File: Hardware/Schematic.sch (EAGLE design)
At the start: 48 parts, among them IC1 XC6220A331MR-G, J1 SAMACSYS_PARTS_USB4110-GF-A, J2 FH34SRJ-24S-0.5SH_99_, J4 112A-TAAR-R03_ATTEND, Q1 20V/4.2A/52mΩ/1.4W, Q2 SI1308EDL-T1-GE3, Q3 20V/4.2A/52mΩ/1.4W, U1 ESP32_WROVER_SPARKFUN-IC-POWE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, U2 ESP32-C6-WROOM-1-N8

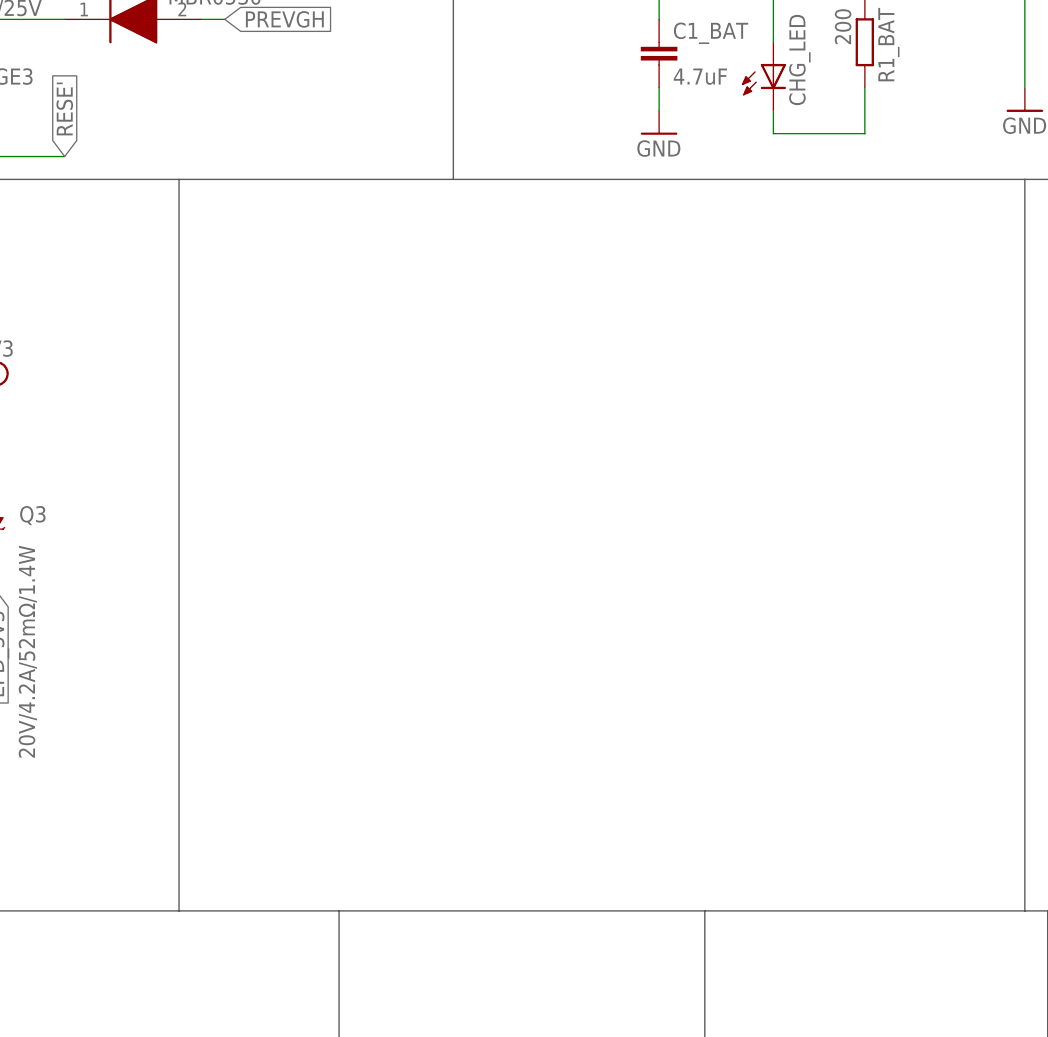
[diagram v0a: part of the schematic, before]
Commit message: add Environmental Sensor BME688
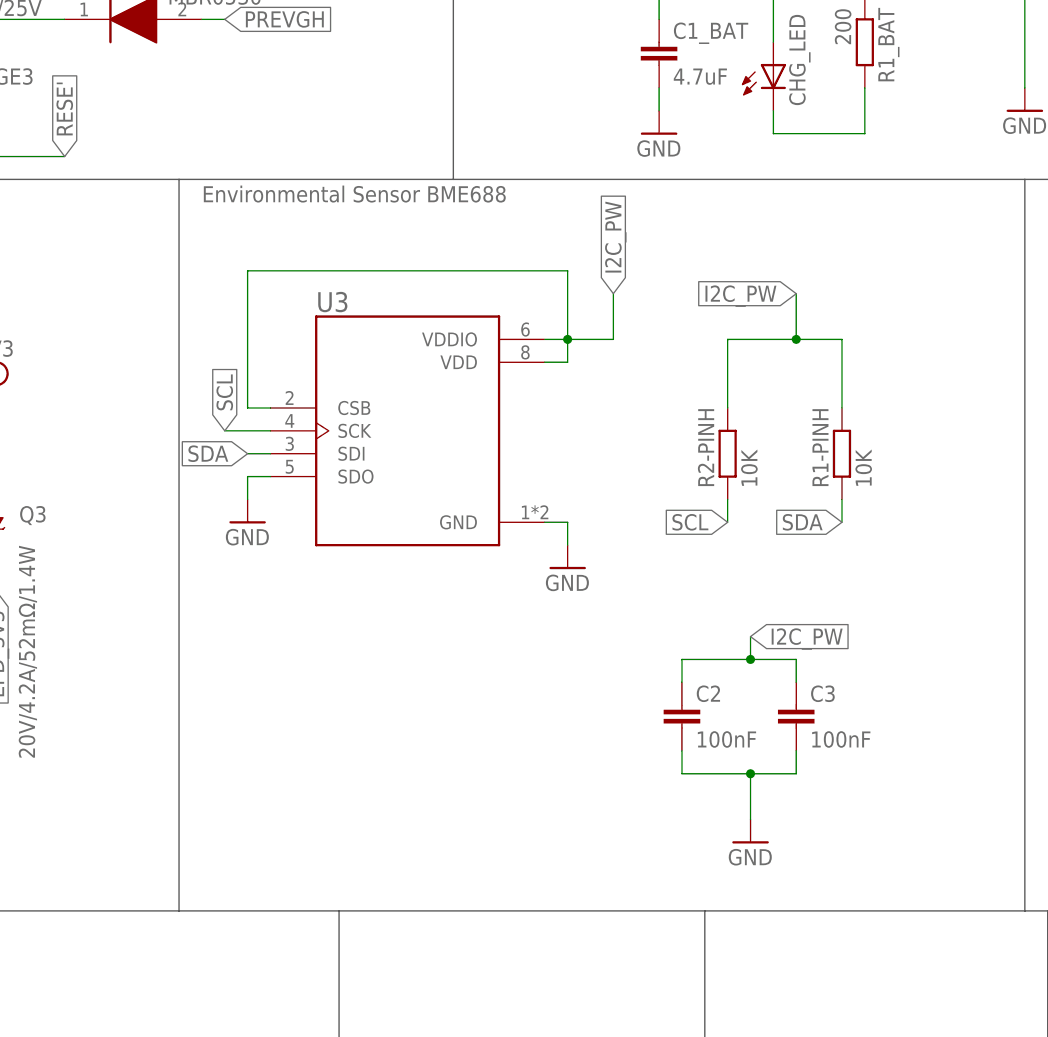
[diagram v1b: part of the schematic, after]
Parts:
- added C2, C3: 100nF, DeskAssistant v19 v1.flbr:ESP32_WROVER_EAGLE-LTSPICE_CC0402
- added R1-PINH, R2-PINH: 10K, DeskAssistant v19 v1.flbr:ESP32_WROVER_EAGLE-LTSPICE_RR0402
- added U3: ESP32_WROVER_BME680_BME680, DeskAssistant v19 v1.flbr:ESP32_WROVER_BME680_BME680
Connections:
- net GND: now also C2.2, C3.2, U3.GND, U3.SDO
- net I2C_PW: now also C2.1, C3.1, R1-PINH.2, R2-PINH.2, U3.CSB, U3.VDD, U3.VDDIO
- net SCL: now also R2-PINH.1, U3.SCK
- net SDA: now also R1-PINH.1, U3.SDI
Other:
- note added: "Environmental Sensor BME688"
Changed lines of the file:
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@@
 <part name="SUPPLY6" library="DeskAssistant v19 v1.flbr" library_urn="urn:adsk.wipprod:fs.file:vf.vVvdDOfaSfavM5thX5SjWw" deviceset="3V3-CIRCLE" device="" value="3V3"/>
 <part name="R_CL1" library="DeskAssistant v19 v1.flbr" library_urn="urn:adsk.wipprod:fs.file:vf.vVvdDOfaSfavM5thX5SjWw" deviceset="ESP32_WROVER_EAGLE-LTSPICE_R" device="R0402" value="10K"/>
+<part name="U3" library="DeskAssistant v19 v1.flbr" library_urn="urn:adsk.wipprod:fs.file:vf.vVvdDOfaSfavM5thX5SjWw" deviceset="ESP32_WROVER_BME680_BME680" device=""/>
+<part name="GND27" library="DeskAssistant v19 v1.flbr" library_urn="urn:adsk.wipprod:fs.file:vf.vVvdDOfaSfavM5thX5SjWw" deviceset="GND" device=""/>
+<part name="GND28" library="DeskAssistant v19 v1.flbr" library_urn="urn:adsk.wipprod:fs.file:vf.vVvdDOfaSfavM5thX5SjWw" deviceset="GND" device=""/>
+<part name="R2-PINH" library="DeskAssistant v19 v1.flbr" library_urn="urn:adsk.wipprod:fs.file:vf.vVvdDOfaSfavM5thX5SjWw" deviceset="ESP32_WROVER_EAGLE-LTSPICE_R" device="R0402" value="10K"/>
+<part name="R1-PINH" library="DeskAssistant v19 v1.flbr" library_urn="urn:adsk.wipprod:fs.file:vf.vVvdDOfaSfavM5thX5SjWw" deviceset="ESP32_WROVER_EAGLE-LTSPICE_R" device="R0402" value="10K"/>
+<part name="C2" library="DeskAssistant v19 v1.flbr" library_urn="urn:adsk.wipprod:fs.file:vf.vVvdDOfaSfavM5thX5SjWw" deviceset="ESP32_WROVER_EAGLE-LTSPICE_C" device="C0402" value="100nF"/>
+<part name="C3" library="DeskAssistant v19 v1.flbr" library_urn="urn:adsk.wipprod:fs.file:vf.vVvdDOfaSfavM5thX5SjWw" deviceset="ESP32_WROVER_EAGLE-LTSPICE_C" device="C0402" value="100nF"/>
+<part name="GND29" library="DeskAssistant v19 v1.flbr" library_urn="urn:adsk.wipprod:fs.file:vf.vVvdDOfaSfavM5thX5SjWw" deviceset="GND" device=""/>
 </parts>
 <sheets>
@@
 <text x="-160.02" y="165.1" size="1.778" layer="95">E-Paper Display Header</text>
 <text x="-73.66" y="162.56" size="1.778" layer="95">EPD Power</text>
+<text x="-27.94" y="165.1" size="1.778" layer="95">Environmental Sensor BME688</text>
 </plain>
 <instances>
@@
 <attribute name="NAME" x="-59.4614" y="146.05" size="1.778" layer="95" rot="R270"/>
 <attribute name="VALUE" x="-64.262" y="146.05" size="1.778" layer="96" rot="R270"/>
+</instance>
+<instance part="U3" gate="G$1" x="-5.08" y="139.7" smashed="yes">
+<attribute name="NAME" x="-15.2493" y="152.92" size="2.186390625" layer="95"/>
+</instance>
+<instance part="GND27" gate="1" x="12.7" y="124.46" smashed="yes">
+<attribute name="VALUE" x="10.16" y="121.92" size="1.778" layer="96"/>
+</instance>
+<instance part="GND28" gate="1" x="-22.86" y="129.54" smashed="yes">
+<attribute name="VALUE" x="-25.4" y="127" size="1.778" layer="96"/>
+</instance>
+<instance part="R2-PINH" gate="G$1" x="30.48" y="137.16" smashed="yes" rot="R90">
+<attribute name="NAME" x="28.9814" y="133.35" size="1.778" layer="95" rot="R90"/>
+<attribute name="VALUE" x="33.782" y="133.35" size="1.778" layer="96" rot="R90"/>
+<attribute name="NAME" x="28.9814" y="133.35" size="1.778" layer="95" rot="R90"/>
+<attribute name="VALUE" x="33.782" y="133.35" size="1.778" layer="96" rot="R90"/>
+</instance>
+<instance part="R1-PINH" gate="G$1" x="43.18" y="137.16" smashed="yes" rot="R90">
+<attribute name="NAME" x="41.6814" y="133.35" size="1.778" layer="95" rot="R90"/>
+<attribute name="VALUE" x="46.482" y="133.35" size="1.778" layer="96" rot="R90"/>
+<attribute name="NAME" x="41.6814" y="133.35" size="1.778" layer="95" rot="R90"/>
+<attribute name="VALUE" x="46.482" y="133.35" size="1.778" layer="96" rot="R90"/>
+</instance>
+<instance part="C2" gate="G$1" x="25.4" y="109.22" smashed="yes">
+<attribute name="NAME" x="26.924" y="109.601" size="1.778" layer="95"/>
+<attribute name="VALUE" x="26.924" y="104.521" size="1.778" layer="96"/>
+</instance>
+<instance part="C3" gate="G$1" x="38.1" y="109.22" smashed="yes">
+<attribute name="NAME" x="39.624" y="109.601" size="1.778" layer="95"/>
+<attribute name="VALUE" x="39.624" y="104.521" size="1.778" layer="96"/>
+</instance>
+<instance part="GND29" gate="1" x="33.02" y="93.98" smashed="yes">
+<attribute name="VALUE" x="30.48" y="91.44" size="1.778" layer="96"/>
 </instance>
 </instances>
@@
 <wire x1="-147.32" y1="144.78" x2="-149.86" y2="144.78" width="0.1524" layer="91"/>
 <pinref part="GND24" gate="1" pin="GND"/>
+</segment>
+<segment>
+<pinref part="U3" gate="G$1" pin="GND"/>
+<wire x1="10.16" y1="129.54" x2="12.7" y2="129.54" width="0.1524" layer="91"/>
+<wire x1="12.7" y1="129.54" x2="12.7" y2="127" width="0.1524" layer="91"/>
+<pinref part="GND27" gate="1" pin="GND"/>
+</segment>
+<segment>
+<pinref part="U3" gate="G$1" pin="SDO"/>
+<wire x1="-20.32" y1="134.62" x2="-22.86" y2="134.62" width="0.1524" layer="91"/>
+<wire x1="-22.86" y1="134.62" x2="-22.86" y2="132.08" width="0.1524" layer="91"/>
+<pinref part="GND28" gate="1" pin="GND"/>
+</segment>
+<segment>
+<pinref part="C2" gate="G$1" pin="2"/>
+<wire x1="25.4" y1="104.14" x2="25.4" y2="101.6" width="0.1524" layer="91"/>
+<wire x1="25.4" y1="101.6" x2="33.02" y2="101.6" width="0.1524" layer="91"/>
+<wire x1="33.02" y1="101.6" x2="38.1" y2="101.6" width="0.1524" layer="91"/>
+<wire x1="38.1" y1="101.6" x2="38.1" y2="104.14" width="0.1524" layer="91"/>
+<pinref part="C3" gate="G$1" pin="2"/>
+<junction x="33.02" y="101.6"/>
+<wire x1="33.02" y1="101.6" x2="33.02" y2="96.52" width="0.1524" layer="91"/>
+<pinref part="GND29" gate="1" pin="GND"/>
 </segment>
 </net>
@@
 <label x="190.5" y="195.58" size="1.778" layer="95" xref="yes"/>
 </segment>
+<segment>
+<pinref part="U3" gate="G$1" pin="VDDIO"/>
+<wire x1="10.16" y1="149.86" x2="12.7" y2="149.86" width="0.1524" layer="91"/>
+<wire x1="12.7" y1="149.86" x2="17.78" y2="149.86" width="0.1524" layer="91"/>
+<wire x1="17.78" y1="149.86" x2="17.78" y2="154.94" width="0.1524" layer="91"/>
+<pinref part="U3" gate="G$1" pin="VDD"/>
+<wire x1="10.16" y1="147.32" x2="12.7" y2="147.32" width="0.1524" layer="91"/>
+<wire x1="12.7" y1="147.32" x2="12.7" y2="149.86" width="0.1524" layer="91"/>
+<junction x="12.7" y="149.86"/>
+<wire x1="12.7" y1="149.86" x2="12.7" y2="157.48" width="0.1524" layer="91"/>
+<wire x1="12.7" y1="157.48" x2="-22.86" y2="157.48" width="0.1524" layer="91"/>
+<wire x1="-22.86" y1="157.48" x2="-22.86" y2="142.24" width="0.1524" layer="91"/>
+<wire x1="-22.86" y1="142.24" x2="-20.32" y2="142.24" width="0.1524" layer="91"/>
+<pinref part="U3" gate="G$1" pin="CSB"/>
+<label x="17.78" y="154.94" size="1.778" layer="95" rot="R90" xref="yes"/>
+</segment>
+<segment>
+<pinref part="R2-PINH" gate="G$1" pin="2"/>
+<wire x1="30.48" y1="142.24" x2="30.48" y2="149.86" width="0.1524" layer="91"/>
+<wire x1="30.48" y1="149.86" x2="38.1" y2="149.86" width="0.1524" layer="91"/>
+<wire x1="38.1" y1="149.86" x2="43.18" y2="149.86" width="0.1524" layer="91"/>
+<wire x1="43.18" y1="149.86" x2="43.18" y2="142.24" width="0.1524" layer="91"/>
+<pinref part="R1-PINH" gate="G$1" pin="2"/>
+<junction x="38.1" y="149.86"/>
+<wire x1="38.1" y1="149.86" x2="38.1" y2="154.94" width="0.1524" layer="91"/>
+<label x="38.1" y="154.94" size="1.778" layer="95" rot="R180" xref="yes"/>
+</segment>
+<segment>
+<pinref part="C2" gate="G$1" pin="1"/>
+<wire x1="25.4" y1="111.76" x2="25.4" y2="114.3" width="0.1524" layer="91"/>
+<wire x1="25.4" y1="114.3" x2="33.02" y2="114.3" width="0.1524" layer="91"/>
+<wire x1="33.02" y1="114.3" x2="38.1" y2="114.3" width="0.1524" layer="91"/>
+<wire x1="38.1" y1="114.3" x2="38.1" y2="111.76" width="0.1524" layer="91"/>
+<pinref part="C3" gate="G$1" pin="1"/>
+<junction x="33.02" y="114.3"/>
+<wire x1="33.02" y1="114.3" x2="33.02" y2="116.84" width="0.1524" layer="91"/>
+<label x="33.02" y="116.84" size="1.778" layer="95" xref="yes"/>
+</segment>
 </net>
 <net name="EPD_3V3_C" class="0">
@@
 <label x="190.5" y="190.5" size="1.778" layer="95" xref="yes"/>
 </segment>
+<segment>
+<pinref part="U3" gate="G$1" pin="SDI"/>
+<wire x1="-20.32" y1="137.16" x2="-22.86" y2="137.16" width="0.1524" layer="91"/>
+<label x="-22.86" y="137.16" size="1.778" layer="95" rot="R180" xref="yes"/>
+</segment>
+<segment>
+<pinref part="R1-PINH" gate="G$1" pin="1"/>
+<wire x1="43.18" y1="132.08" x2="43.18" y2="129.54" width="0.1524" layer="91"/>
+<label x="43.18" y="129.54" size="1.778" layer="95" rot="R180" xref="yes"/>
+</segment>
 </net>
 <net name="SCL" class="0">
@@
 <label x="190.5" y="187.96" size="1.778" layer="95" xref="yes"/>
 </segment>
-</net>
+<segment>
+<pinref part="U3" gate="G$1" pin="SCK"/>
+<label x="-25.4" y="139.7" size="1.778" layer="95" rot="R90" xref="yes"/>
+<wire x1="-20.32" y1="139.7" x2="-25.4" y2="139.7" width="0.1524" layer="91"/>
+</segment>
+<segment>
+<pinref part="R2-PINH" gate="G$1" pin="1"/>
+<wire x1="30.48" y1="132.08" x2="30.48" y2="129.54" width="0.1524" layer="91"/>
+<label x="30.48" y="129.54" size="1.778" layer="95" rot="R180" xref="yes"/>
+</segment>
+</net>

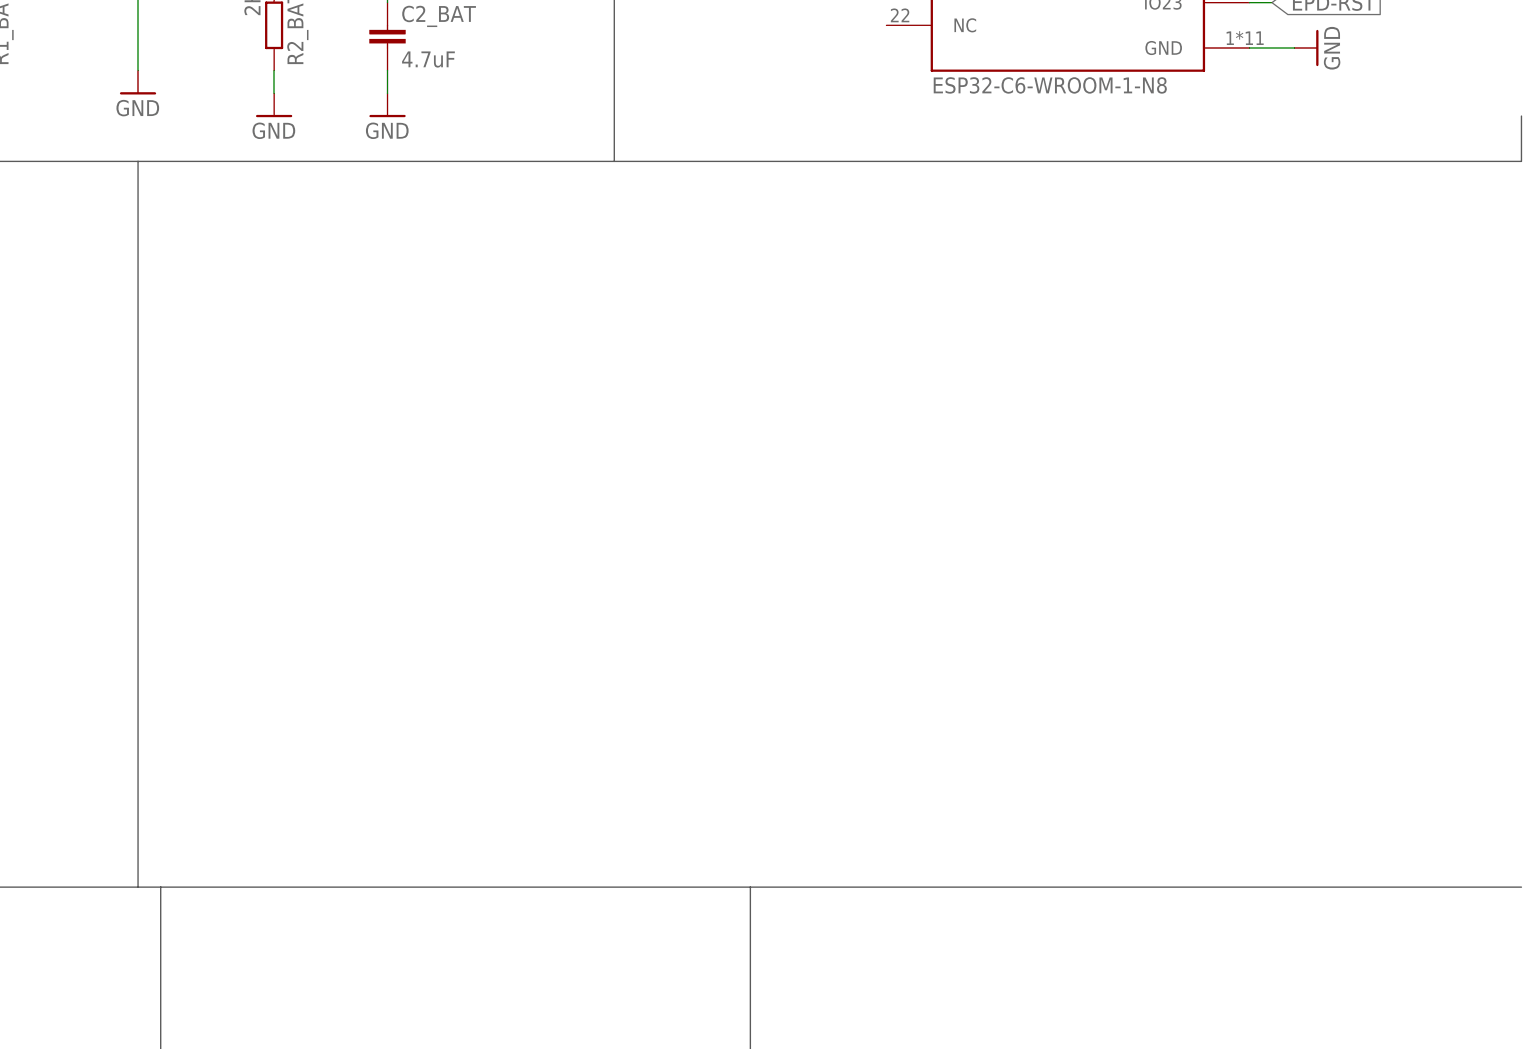
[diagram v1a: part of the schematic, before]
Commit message: add Voltage Supervisor + Reset & Boot / IO Button
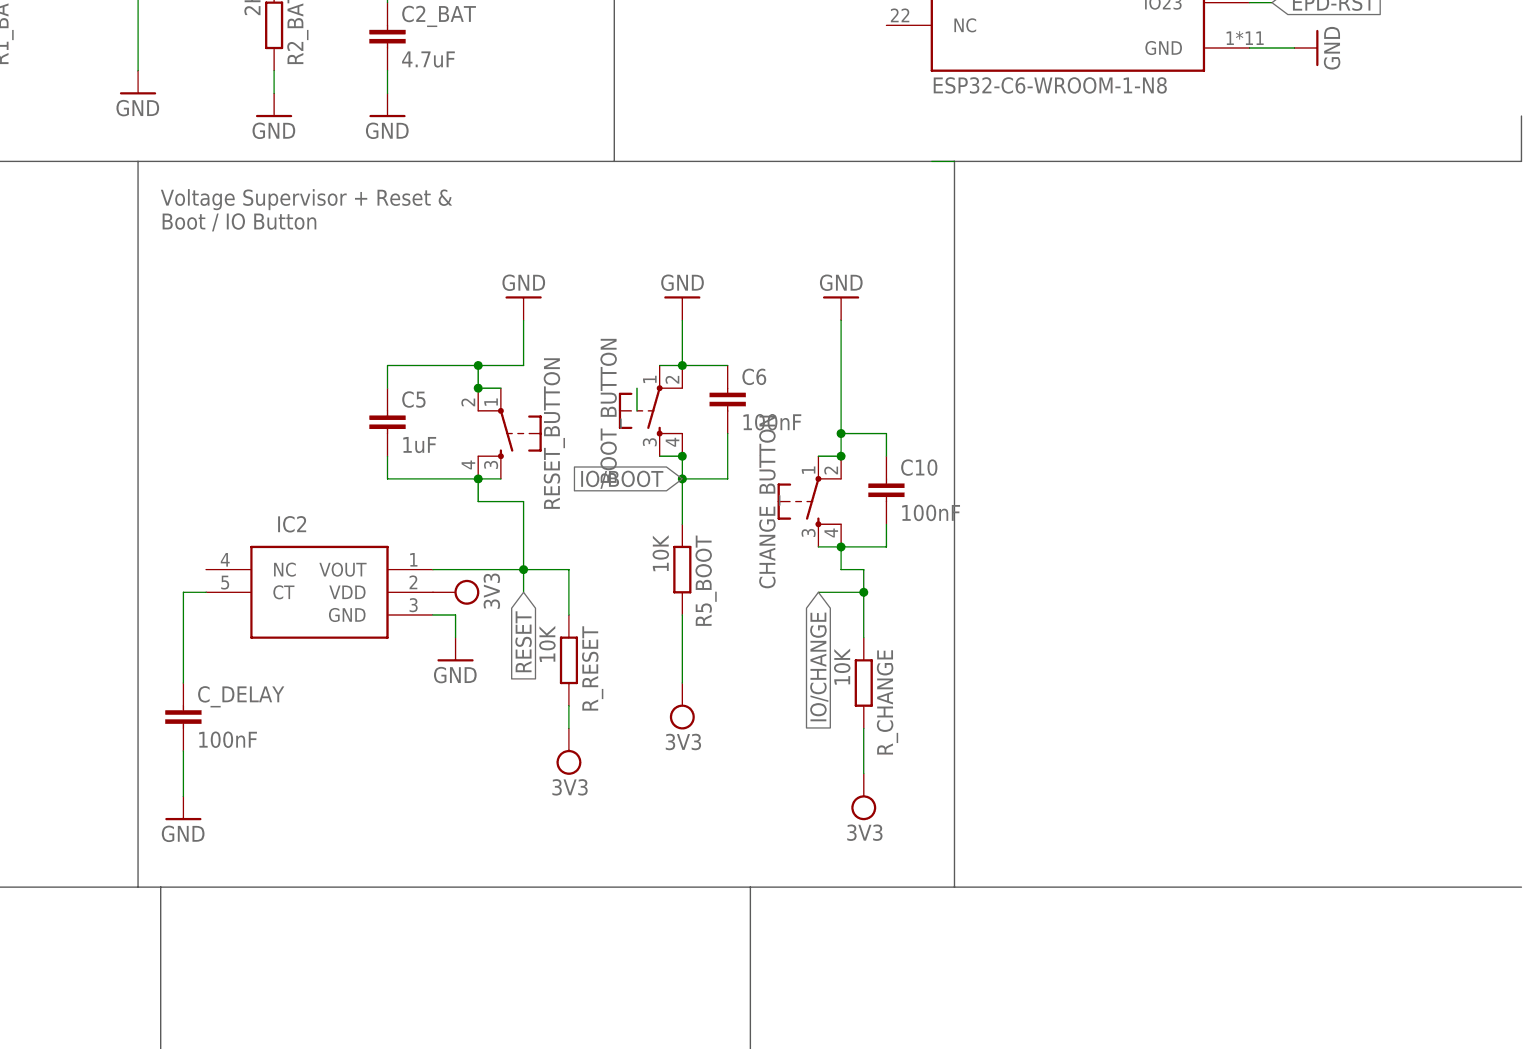
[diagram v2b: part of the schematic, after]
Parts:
- added BOOT_BUTTON, CHANGE_BUTTON, RESET_BUTTON: BUTTON_CUSYOMV1, DeskAssistant v19 v1.flbr:BUTTON_CUSYOMV1
- added C10, C6: 100nF, DeskAssistant v19 v1.flbr:ESP32_WROVER_EAGLE-LTSPICE_CC0402
- added C5: 1uF, DeskAssistant v19 v1.flbr:ESP32_WROVER_EAGLE-LTSPICE_CC0402
- added C_DELAY: 100nF, DeskAssistant v19 v1.flbr:EAGLE-LTSPICE_CC0402
- added IC2: BD5229G-TR, DeskAssistant v19 v1.flbr:BD5229G-TR
- added R5_BOOT, R_CHANGE, R_RESET: 10K, DeskAssistant v19 v1.flbr:ESP32_WROVER_EAGLE-LTSPICE_RR0402
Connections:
- new net N$19: C_DELAY.1, IC2.CT
- net 3V3: now also IC2.VDD, R5_BOOT.2, R_CHANGE.2, R_RESET.2
- net GND: now also BOOT_BUTTON.1, BOOT_BUTTON.2, C10.1, C5.1, C6.1, CHANGE_BUTTON.1, CHANGE_BUTTON.2, C_DELAY.2, IC2.GND, RESET_BUTTON.1, RESET_BUTTON.2
- net IO/BOOT: now also BOOT_BUTTON.3, BOOT_BUTTON.4, C6.2, R5_BOOT.1
- net IO/CHANGE: now also C10.2, CHANGE_BUTTON.3, CHANGE_BUTTON.4, R_CHANGE.1
- net RESET: now also C5.2, IC2.VOUT, RESET_BUTTON.3, RESET_BUTTON.4, R_RESET.1
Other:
- note added: "Voltage Supervisor + Reset & Boot / IO Button"
